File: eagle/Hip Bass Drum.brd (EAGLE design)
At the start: 66 x 69.5 mm, 40 parts, among them IC1 LM4558N, T1 2N3904

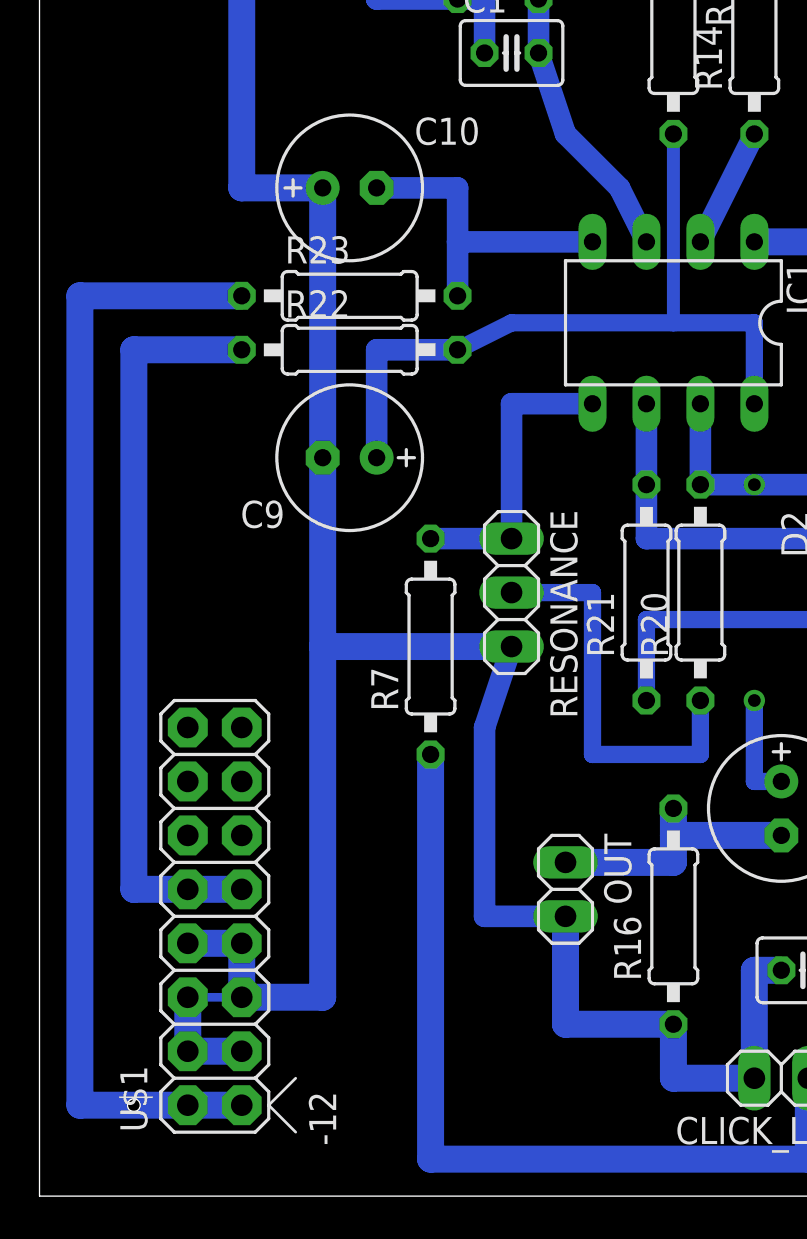
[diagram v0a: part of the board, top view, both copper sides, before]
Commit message: removed the drill on the new trace
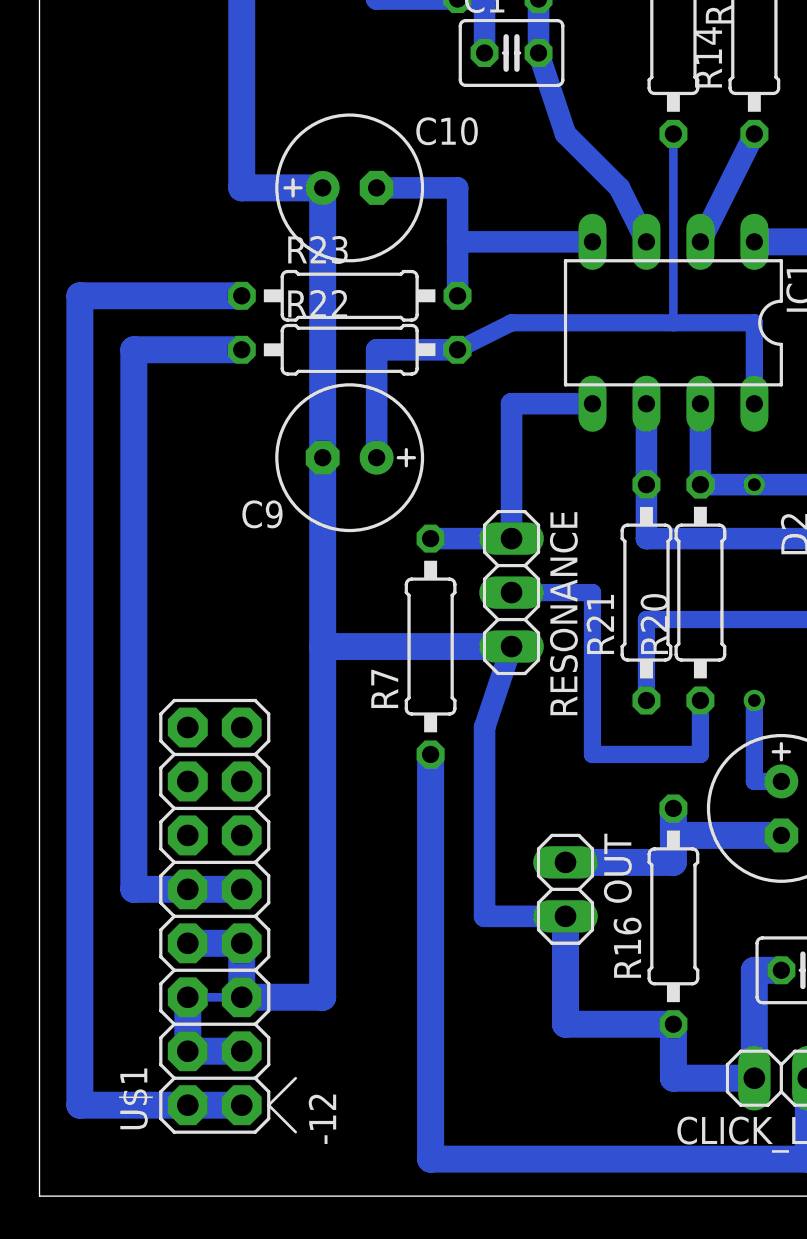
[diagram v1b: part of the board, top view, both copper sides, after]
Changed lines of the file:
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@@
 <wire x1="66.66" y1="70.32" x2="0.64" y2="70.32" width="0" layer="20"/>
 <wire x1="0.64" y1="70.32" x2="0.64" y2="0.8" width="0" layer="20"/>
-<hole x="5.08" y="5.08" drill="0.6"/>
 <hole x="5.08" y="66.04" drill="0.6"/>
 <hole x="62.23" y="66.04" drill="0.6"/>
@@
 <wire x1="16.51" y1="40.64" x2="20.32" y2="40.64" width="1.016" layer="16"/>
 <wire x1="16.51" y1="35.56" x2="16.51" y2="40.64" width="1.016" layer="16"/>
-<wire x1="30.48" y1="41.91" x2="30.48" y2="50.8" width="0.6096" layer="16"/>
+<wire x1="30.48" y1="41.91" x2="30.48" y2="50.8" width="0.4064" layer="16"/>
 </signal>
 <signal name="V-">
@@
 <signal name="N$4">
 <contactref element="R22" pad="1"/>
-<wire x1="10.16" y1="39.37" x2="10.16" y2="40.64" width="0" layer="19" extent="1-16"/>
 <contactref element="U$1" pad="9"/>
 <contactref element="U$1" pad="10"/>
@@
 <signal name="N$5">
 <contactref element="R23" pad="1"/>
-<wire x1="10.16" y1="43.18" x2="10.16" y2="44.45" width="0" layer="19" extent="1-16"/>
 <contactref element="U$1" pad="2"/>
 <contactref element="U$1" pad="1"/>
@@
 <wire x1="43.18" y1="31.75" x2="45.72" y2="29.21" width="1.016" layer="16"/>
 <wire x1="45.72" y1="29.21" x2="49.53" y2="29.21" width="1.016" layer="16"/>
+<via x="49.53" y="35.56" extent="1-16" drill="0.6" shape="square"/>
 <wire x1="49.53" y1="29.21" x2="49.53" y2="35.56" width="0" layer="19" extent="16-16"/>
-<via x="49.53" y="35.56" extent="1-16" drill="0.6" shape="square"/>
 </signal>
 <signal name="N$15">
@@
 <wire x1="55.88" y1="40.64" x2="59.69" y2="40.64" width="1.016" layer="16"/>
 <wire x1="55.88" y1="35.56" x2="55.88" y2="40.64" width="1.016" layer="16"/>
-<wire x1="31.75" y1="34.29" x2="34.29" y2="34.29" width="0" layer="19" extent="1-16"/>
 <wire x1="31.75" y1="34.29" x2="45.72" y2="34.29" width="1.016" layer="16"/>
 <wire x1="45.72" y1="34.29" x2="48.26" y2="31.75" width="1.016" layer="16"/>
@@
 <wire x1="34.29" y1="20.32" x2="35.56" y2="20.32" width="0.8128" layer="16"/>
 <wire x1="34.29" y1="20.32" x2="34.29" y2="24.13" width="0.8128" layer="16"/>
-<wire x1="34.29" y1="24.13" x2="34.29" y2="34.29" width="0" layer="19" extent="16-16"/>
+<wire x1="34.29" y1="24.13" x2="31.75" y2="34.29" width="0" layer="19" extent="16-16"/>
 </signal>
 <signal name="N$16">
